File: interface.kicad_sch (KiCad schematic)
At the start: 14 parts, among them J10 Conn_01x05, J11 Conn_DEGSON_01x02_Pin, U9 ST485E

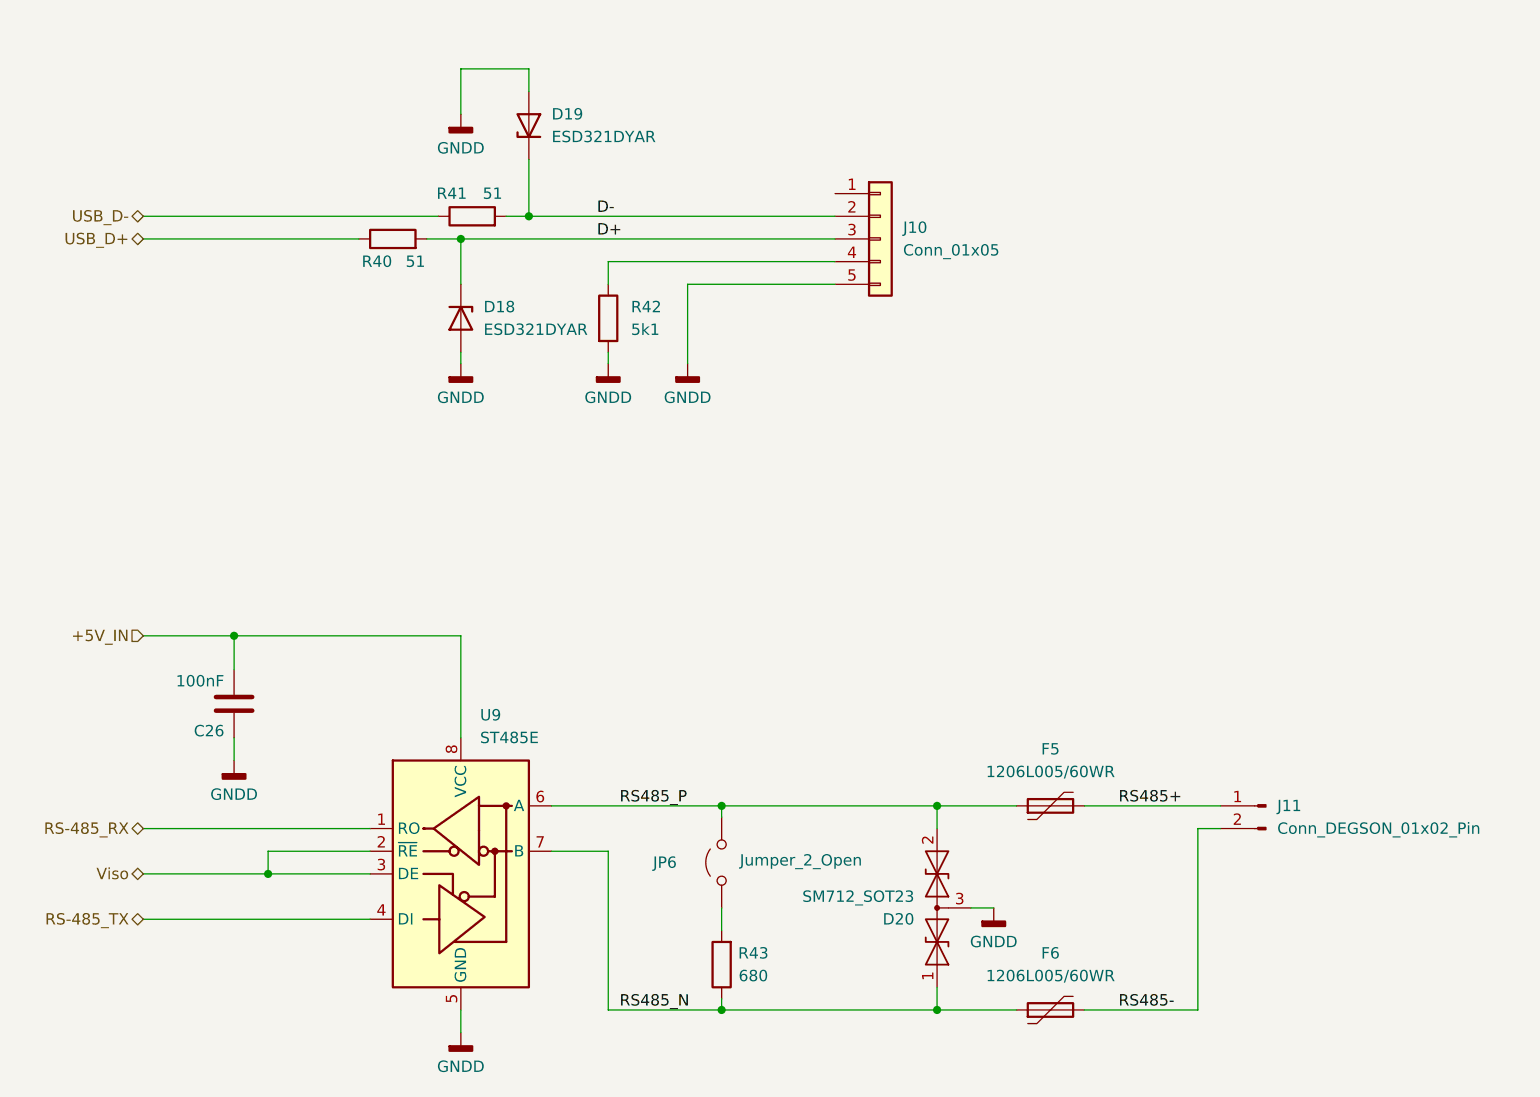
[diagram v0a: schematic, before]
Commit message: USB pinout fixed
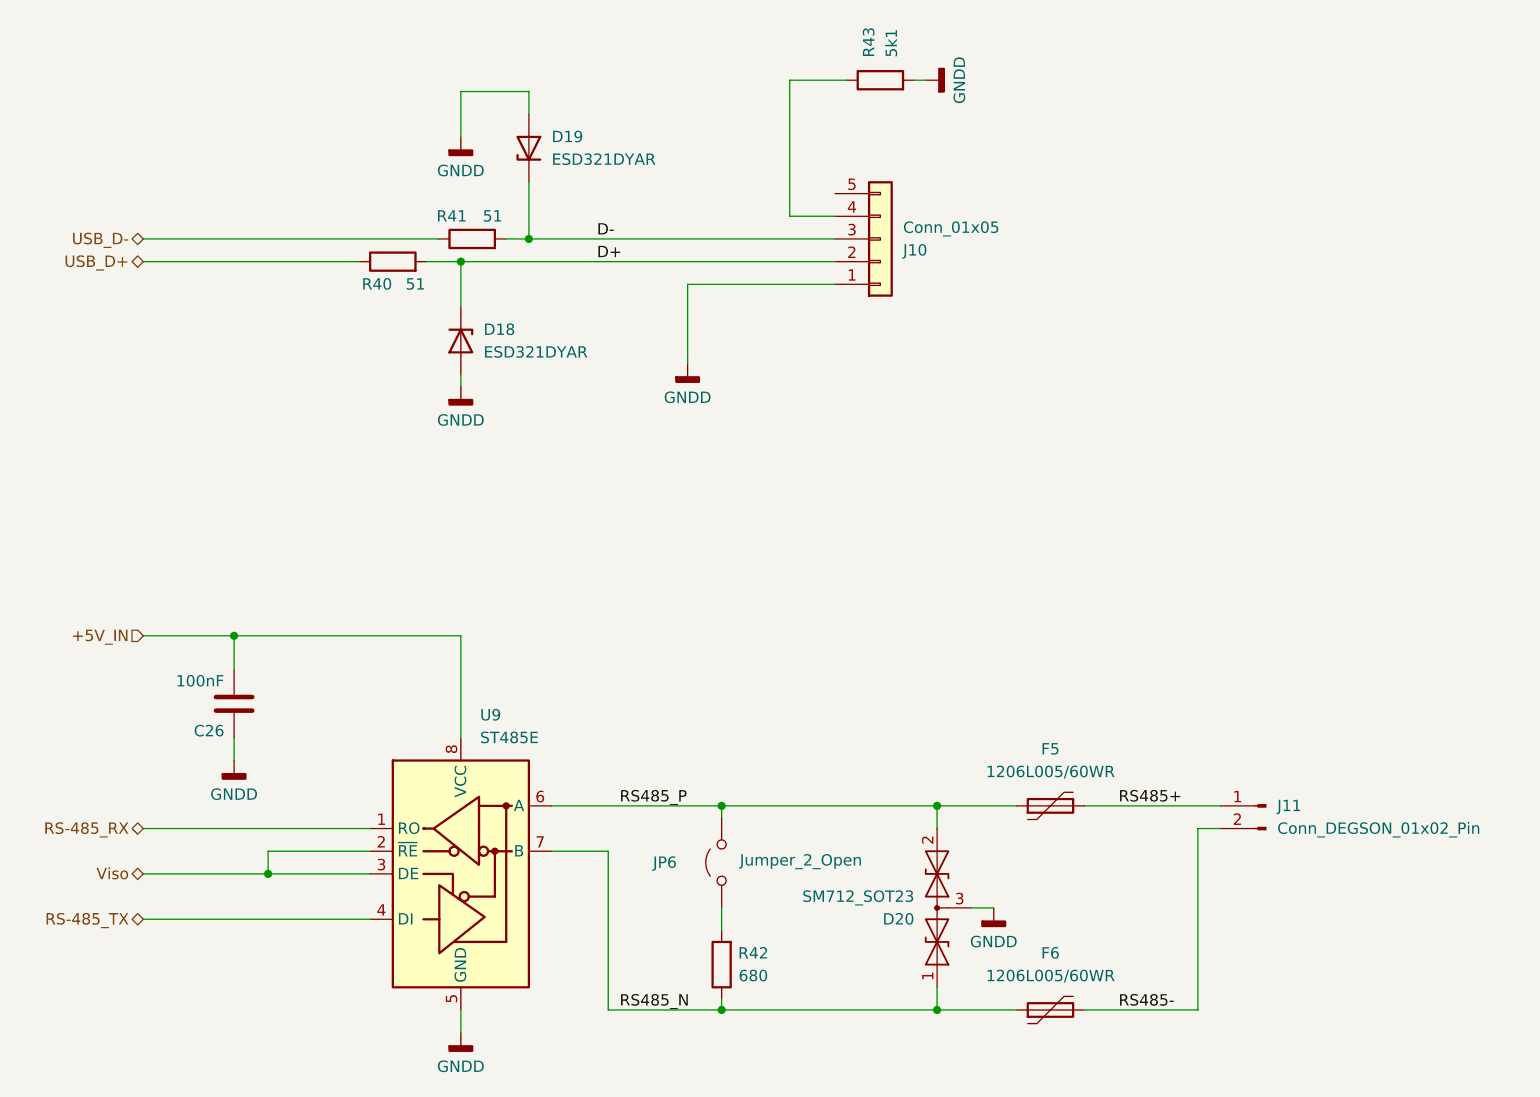
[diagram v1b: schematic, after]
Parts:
- renumbered R43 to R42, R42 to R43
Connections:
- net D+: now also J10.2 (Pin_2); no longer J10.3 (Pin_3)
- net D-: now also J10.3 (Pin_3); no longer J10.2 (Pin_2)
- net GNDD: now also J10.1 (Pin_1); no longer J10.5 (Pin_5)
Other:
- moved on the sheet: D18, D19, R40, R41, R43

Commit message: Move to SIM800C-DS and two SIM
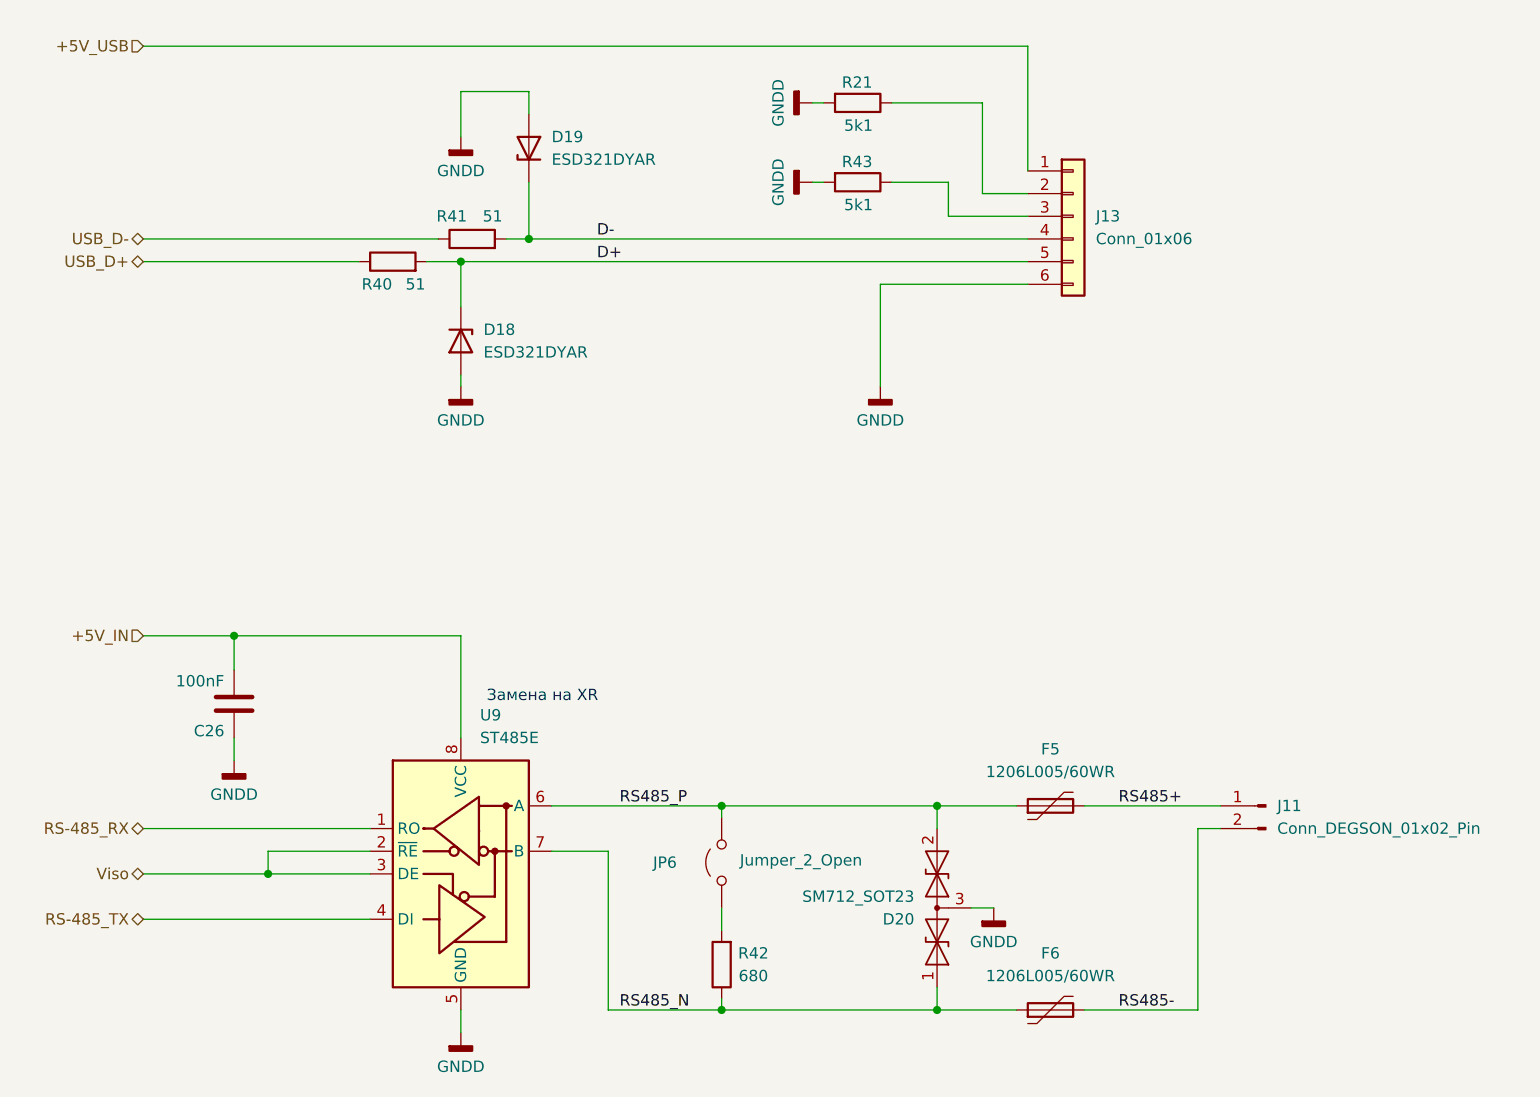
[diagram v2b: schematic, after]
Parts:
- removed J10: Conn_01x05, Connector_JST:JST_PH_B5B-PH-K_1x05_P2.00mm_Vertical, symbol Connector_Generic:Conn_01x05
- added J13: Conn_01x06, Connector_JST:JST_PH_B6B-PH-K_1x06_P2.00mm_Vertical, symbol Connector_Generic:Conn_01x06
- added R21: 5k1, Resistor_SMD:R_0805_2012Metric_Pad1.20x1.40mm_HandSolder, symbol Device:R
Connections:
- net D+: now also J13.5 (Pin_5)
- net D-: now also J13.4 (Pin_4)
- net GNDD: now also J13.6 (Pin_6), R21.2
- net at R43.1: now also J13.3 (Pin_3)
- new net: J13.2 (Pin_2), R21.1
- new net +5V_USB: J13.1 (Pin_1)
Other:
- note added: "Замена на XR"
- moved on the sheet: R43
